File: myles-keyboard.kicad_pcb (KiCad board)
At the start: 2 copper layers, 202.7 x 119.4 mm, 50 parts, among them J1 TRRS, J2 OLED, SW01 Key, SW02 Key, SW03 Key, SW04 Key, SW11 Key, SW12 Key, SW13 Key, SW14 Key, SW15 Key, SW16 Key, SW17 Key, SW18 Key, SW19 Key, SW21 Key, SW22 Key, SW23 Key, SW24 Key, SW25 Key, SW26 Key, SW27 Key, SW28 Key, SW29 Key, SW30 Key, SW31 Key, SW32 Key, SW33 Key, SW34 Key, SW35 Key, SW36 Key, SW37 Key, SW38 Key, SW39 Key, SW40 Key, SW41 Key, SW42 Key, SW43 Key, SW44 Key, SW45 Key, SW46 Key, SW47 Key, SW48 Key, SW49 Key, U1 ProMicro

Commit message: added new jumpers
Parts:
- moved SW_RST1 5.12 mm to (-64.2, 19.9)
- moved U1 1.80 mm to (-58.3, -0.38)
- moved J2 1.62 mm to (-56.8, 18.1)
- moved J1 1.14 mm to (-68.3, 40.5)
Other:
- board size 202.7 x 119.4 mm -> 203 x 275.4 mm

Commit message: rotate keyboard
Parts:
- removed R1, R2: R, myles-keyboard:R
- added JP10: Jumper_2_Open, myles-keyboard:Jumper, F.Cu at (13.2, 125.7)
- added JP3: Jumper_2_Open, myles-keyboard:Jumper, F.Cu at (13.2, 104.7)
- added JP4: Jumper_2_Open, myles-keyboard:Jumper, F.Cu at (13.2, 107.7)
- added JP5: Jumper_2_Open, myles-keyboard:Jumper, F.Cu at (13.2, 110.7)
- added JP6: Jumper_2_Open, myles-keyboard:Jumper, F.Cu at (13.2, 113.7)
- added JP7: Jumper_2_Open, myles-keyboard:Jumper, F.Cu at (13.2, 116.7)
- added JP8: Jumper_2_Open, myles-keyboard:Jumper, F.Cu at (13.2, 119.7)
- added JP9: Jumper_2_Open, myles-keyboard:Jumper, F.Cu at (13.2, 122.7)
- moved SW19 144.7 mm to (234.5, 75.6), turned to -10 degrees
- moved SW18 143.9 mm to (216.7, 72.5), turned to -10 degrees
- moved SW29 143.4 mm to (231.5, 92.4), turned to -10 degrees
- moved SW17 143.2 mm to (199.0, 69.4), turned to -10 degrees
- moved SW28 142.6 mm to (213.8, 89.3), turned to -10 degrees
- moved SW16 142.6 mm to (180.7, 65.3), turned to -15 degrees
- moved SW39 142.1 mm to (228.6, 109.1), turned to -10 degrees
- moved SW04 142.0 mm to (143.2, 46.5), turned to -10 degrees
- moved SW15 142.0 mm to (163.4, 60.7), turned to -15 degrees
- moved SW27 141.9 mm to (196.1, 86.1), turned to -10 degrees
- moved SW03 141.5 mm to (120.9, 39.4), turned to -5 degrees
- moved SW38 141.3 mm to (210.8, 106.0), turned to -10 degrees
- moved SW26 141.2 mm to (176.3, 81.8), turned to -15 degrees
- moved SW49 140.7 mm to (225.6, 125.9), turned to -10 degrees
- moved SW14 140.7 mm to (140.2, 63.2), turned to -10 degrees
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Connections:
- J2 pad 1: GND -> Net-(JP3-B)
- J2 pad 2: VCC -> Net-(JP4-B)
- J2 pad 3: SCL -> Net-(JP5-B)
- J2 pad 4: SDA -> Net-(JP10-B)
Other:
- board size 203 x 275.4 mm -> 209.1 x 275.4 mm

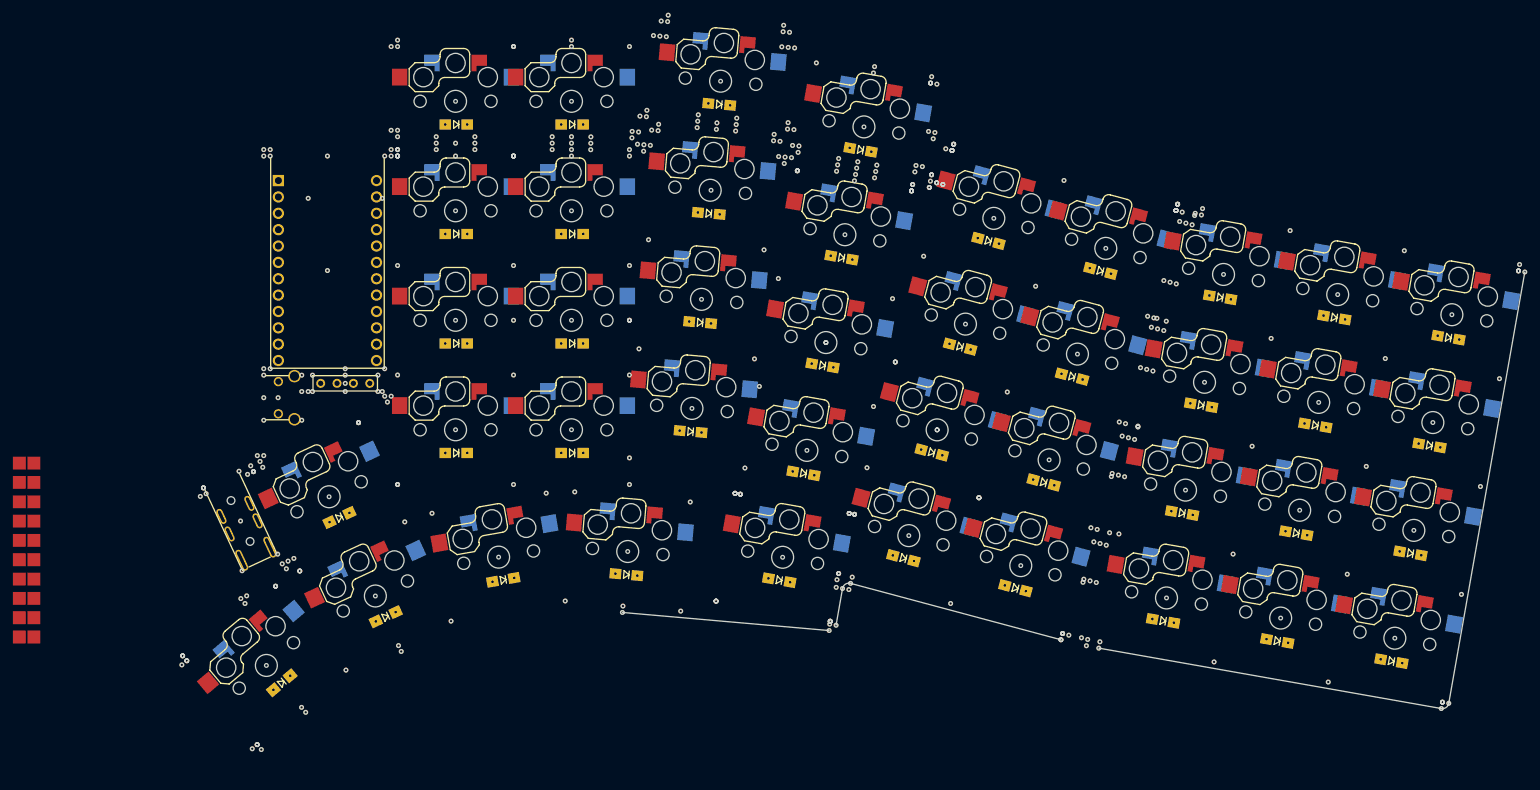
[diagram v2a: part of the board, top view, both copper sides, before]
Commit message: move footprints
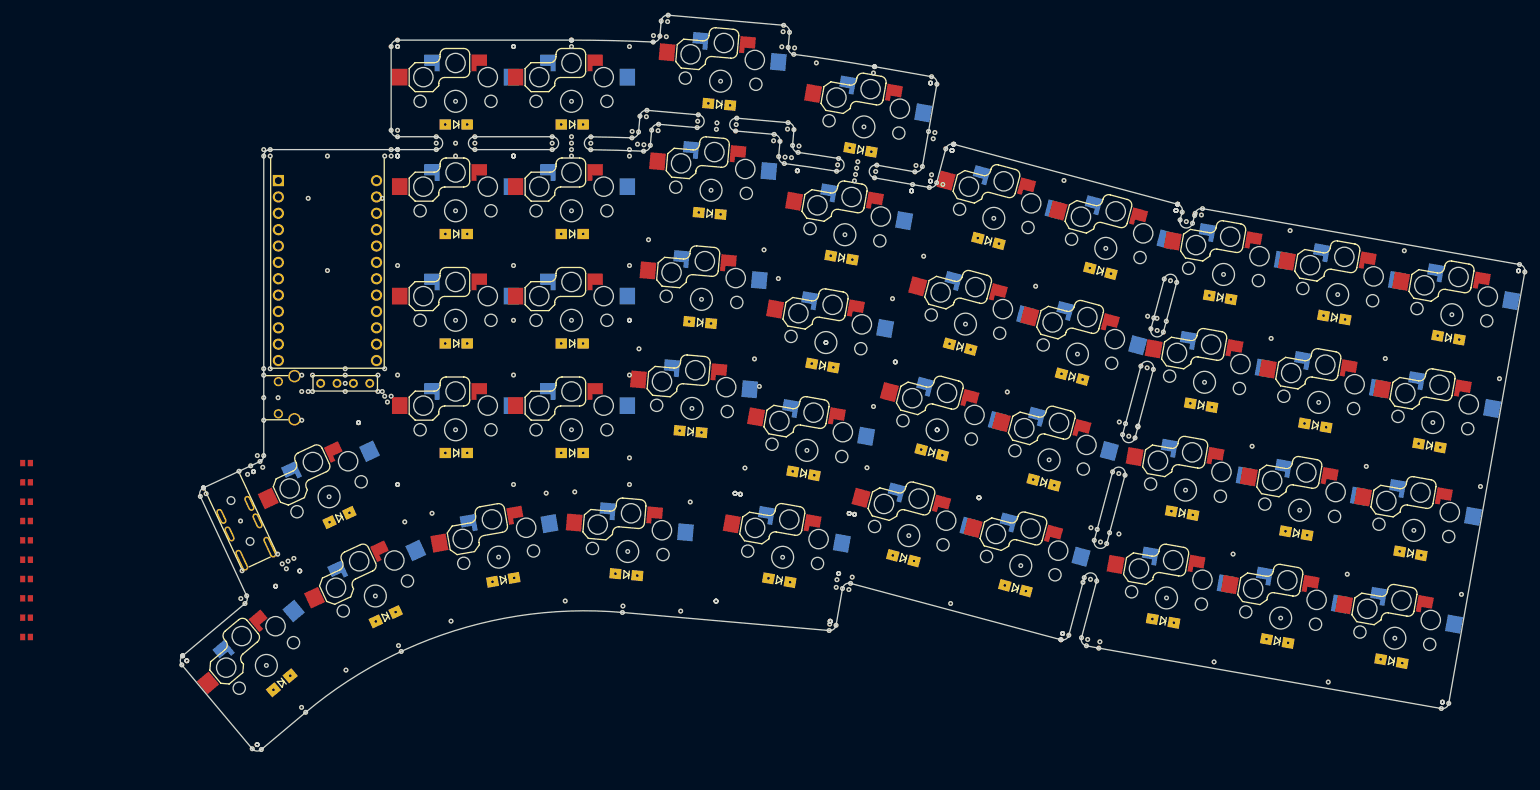
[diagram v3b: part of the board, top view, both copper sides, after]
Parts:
- moved SW13 0.13 mm to (119.4, 56.3)
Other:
- outline, holes or cut-outs redrawn

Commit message: everything but pads in position
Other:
- board size 209.1 x 275.4 mm -> 208.8 x 114.3 mm
